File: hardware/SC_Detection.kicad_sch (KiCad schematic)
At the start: 86 parts, among them U23 LT1678CS8#PBF, U24 LT1678CS8#PBF, U25 LM211DRG4, U26 LM211DRG4, U27 LM211DRG4, U28 LM211DRG4

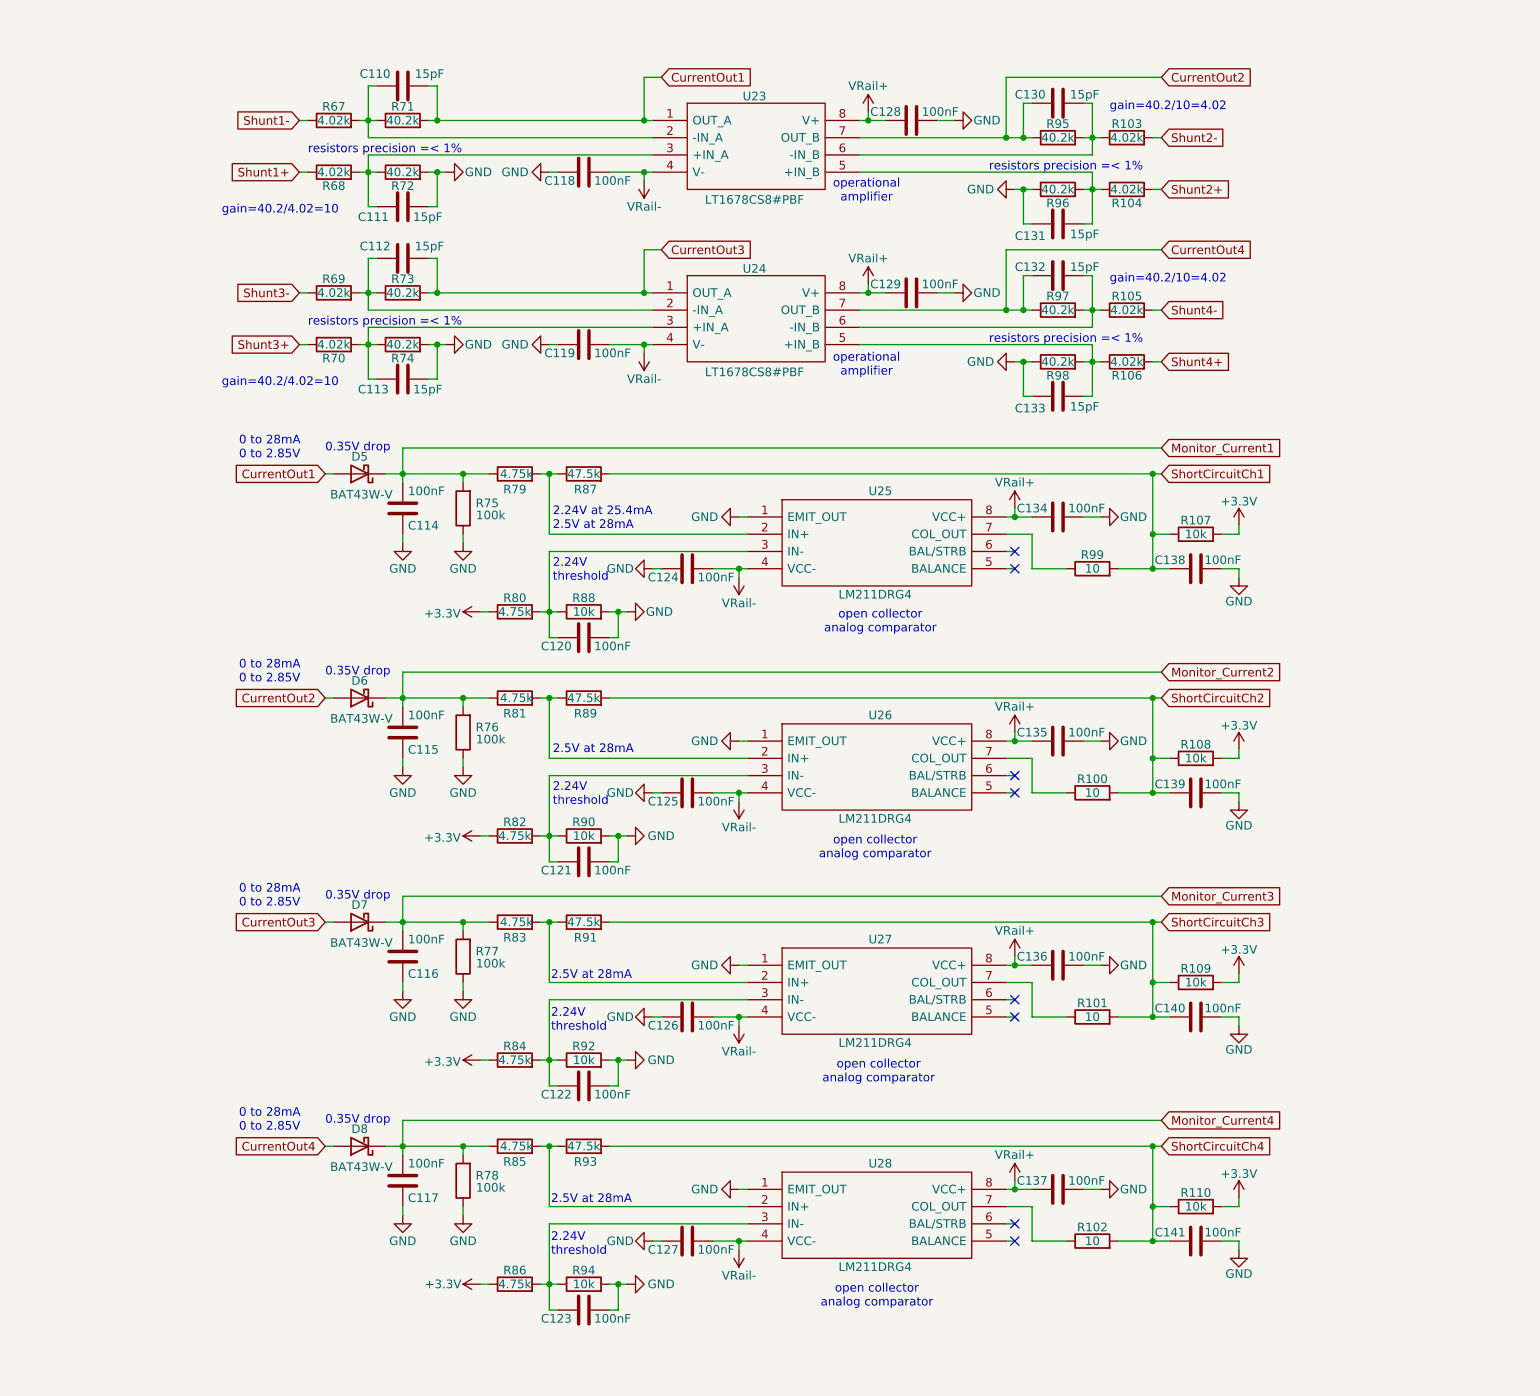
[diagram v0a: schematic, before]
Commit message: Added caps voltage rating + block diagram
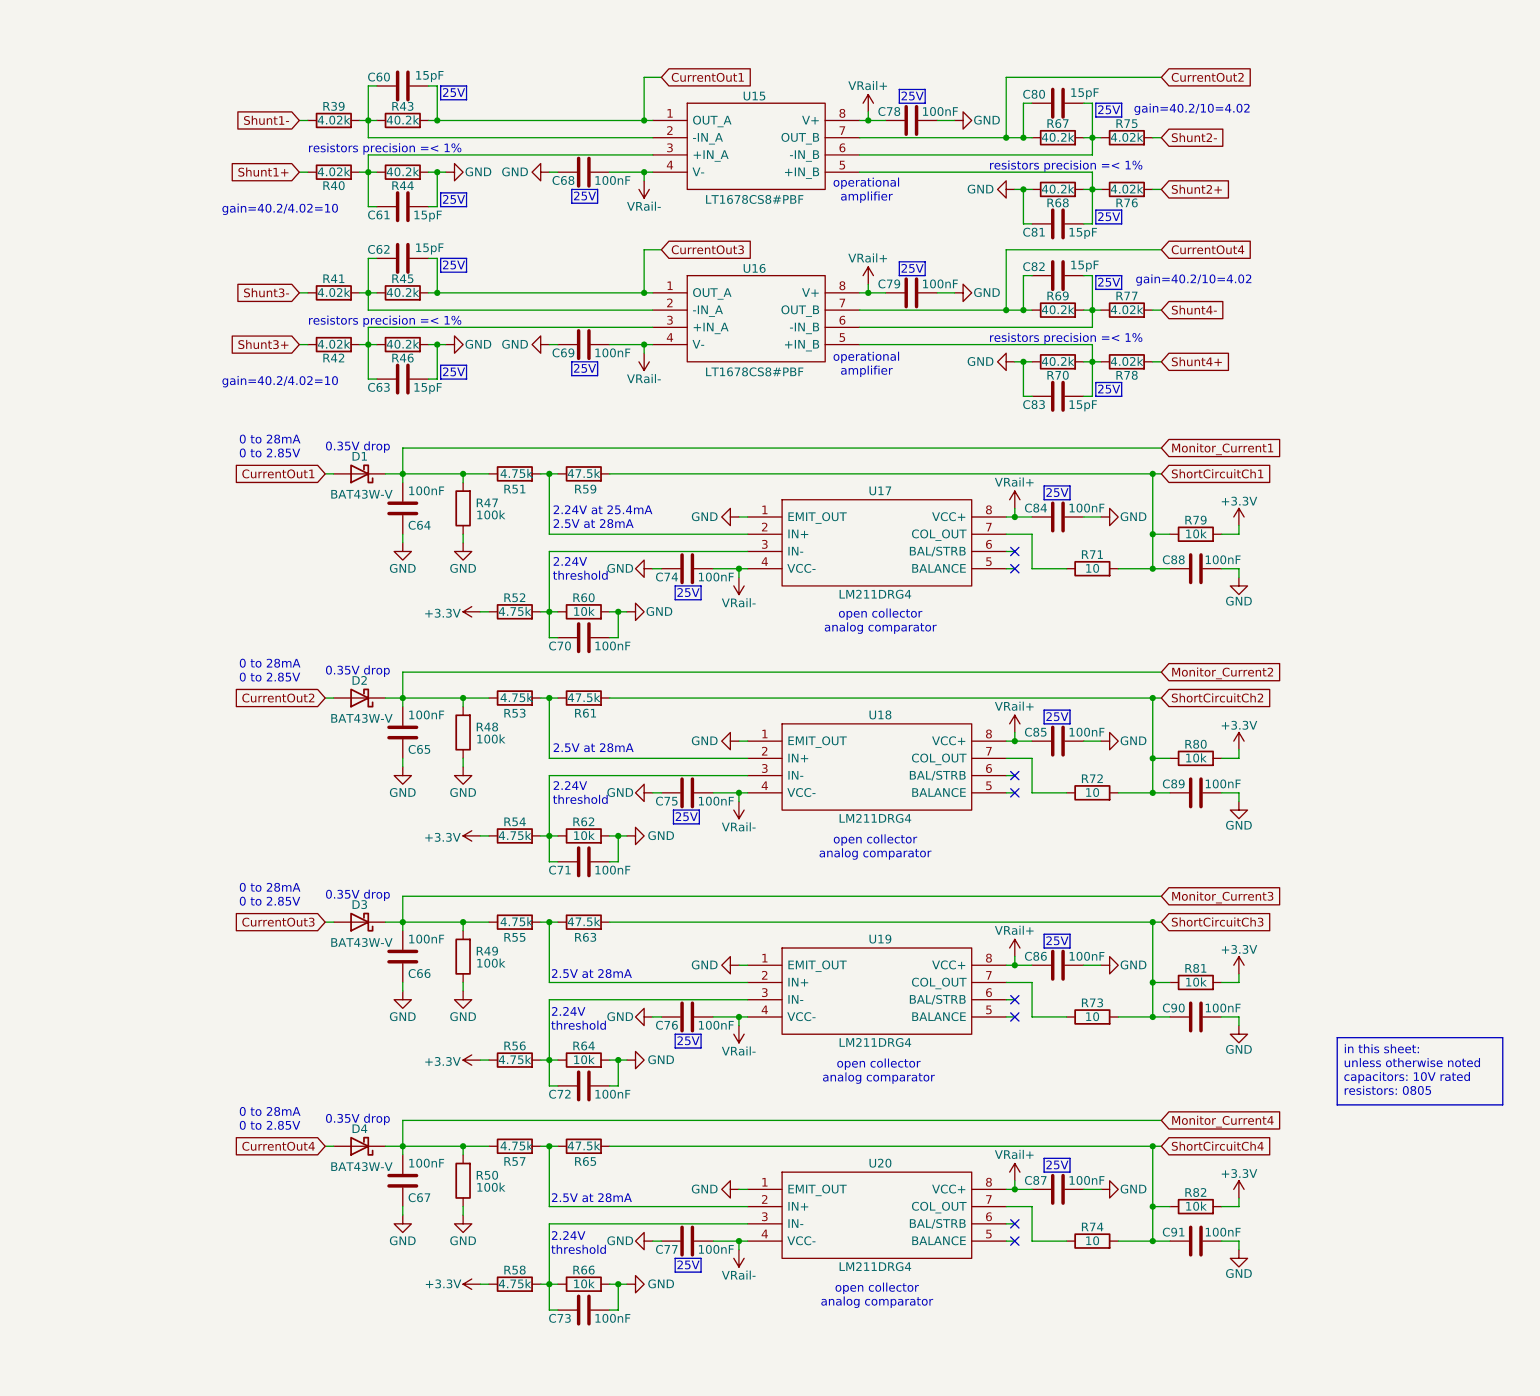
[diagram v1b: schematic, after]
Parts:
- removed C112, C113, C130, C131, C132, C133: 15pF, Capacitor_SMD:C_0402_1005Metric, symbol Device:C
- added C62, C63, C80, C81, C82, C83: 15pF, Capacitor_SMD:C_0402_1005Metric, symbol Device:C
- renumbered C110 to C60, C111 to C61, C114 to C64, C115 to C65, C116 to C66, C117 to C67, C118 to C68, C119 to C69, C120 to C70, C121 to C71, C122 to C72, C123 to C73, C124 to C74, C125 to C75, C126 to C76, C127 to C77, C128 to C78, C129 to C79, C134 to C84, C135 to C85, C136 to C86, C137 to C87, C138 to C88, C139 to C89, C140 to C90, C141 to C91, D5 to D1, D6 to D2, D7 to D3, D8 to D4, R67 to R39, R68 to R40, R69 to R41, R70 to R42, R71 to R43, R72 to R44, R73 to R45, R74 to R46, R75 to R47, R76 to R48, R77 to R49, R78 to R50, R79 to R51, R80 to R52, R81 to R53, R82 to R54, R83 to R55, R84 to R56, R85 to R57, R86 to R58, R87 to R59, R88 to R60, R89 to R61, R90 to R62, R91 to R63, R92 to R64, R93 to R65, R94 to R66, R95 to R67, R96 to R68, R97 to R69, R98 to R70, R99 to R71, R100 to R72, R101 to R73, R102 to R74, R103 to R75, R104 to R76, R105 to R77, R106 to R78, R107 to R79, R108 to R80, R109 to R81, R110 to R82, U23 to U15, U24 to U16, U25 to U17, U26 to U18, U27 to U19, U28 to U20
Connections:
- net CurrentOut2: now also C80.2
- net CurrentOut3: now also C62.1
- net CurrentOut4: now also C82.2
- net GND: now also C63.1, C81.2, C83.2
- net at R67.2, R75.1, U15.6 (-IN_B): now also C80.1
- net at R69.2, R77.1, U16.6 (-IN_B): now also C82.1
- net at R70.2, R78.1, U16.5 (+IN_B): now also C83.1
- net at R41.2, R45.1, U16.2 (-IN_A): now also C62.2
- net at R68.2, R76.1, U15.5 (+IN_B): now also C81.1
- net at R42.2, R46.1, U16.3 (+IN_A): now also C63.2
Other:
- title: Multi Channel HARP DAC -> harp device quad dac

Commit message: The footprint assigning and reviewing have started.
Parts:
- C60, C61, C62, C63, C64, C65, C66, C67, C68, C69, C70, C71, C72, C73, C74, C75, C76, C77, C78, C79, C80, C81, C82, C83, C84, C85, C86, C87, C88, C89, C90, C91: symbol Device:C -> harp.device.quad.dac:C
- D1, D2, D3, D4: symbol Diode:BAT43W-V -> harp.device.quad.dac:BAT43W-V
- R39, R40, R41, R42, R43, R44, R45, R46, R47, R48, R49, R50, R51, R52, R53, R54, R55, R56, R57, R58, R59, R60, R61, R62, R63, R64, R65, R66, R67, R68, R69, R70, R71, R72, R73, R74, R75, R76, R77, R78, R79, R80, R81, R82: symbol Device:R -> harp.device.quad.dac:R
- U15, U16: symbol LT1678CS8#PBF:LT1678CS8#PBF -> harp.device.quad.dac:LT1678CS8#PBF
- U17, U18, U19, U20: symbol LM211DRG4:LM211DRG4 -> harp.device.quad.dac:LM211DRG4

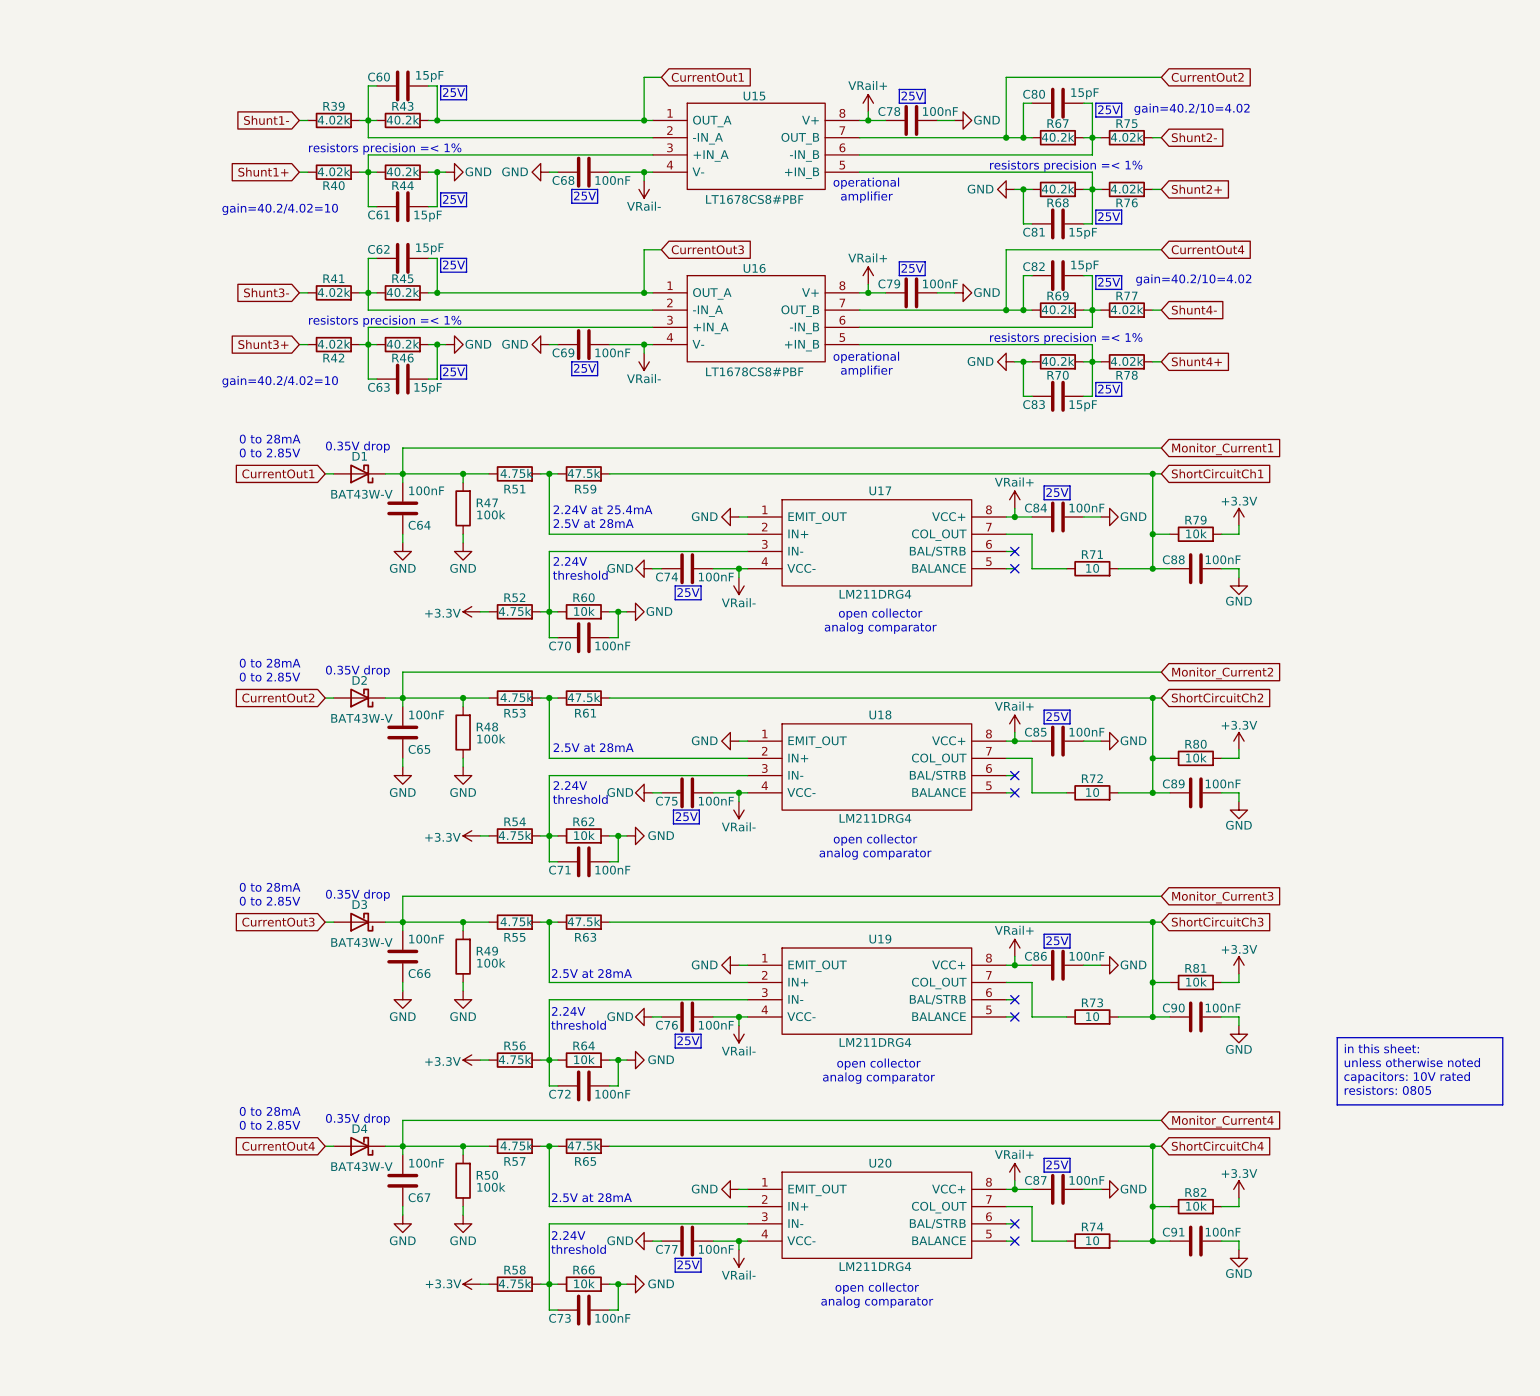
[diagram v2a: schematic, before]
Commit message: Modified notes about caps and resistors
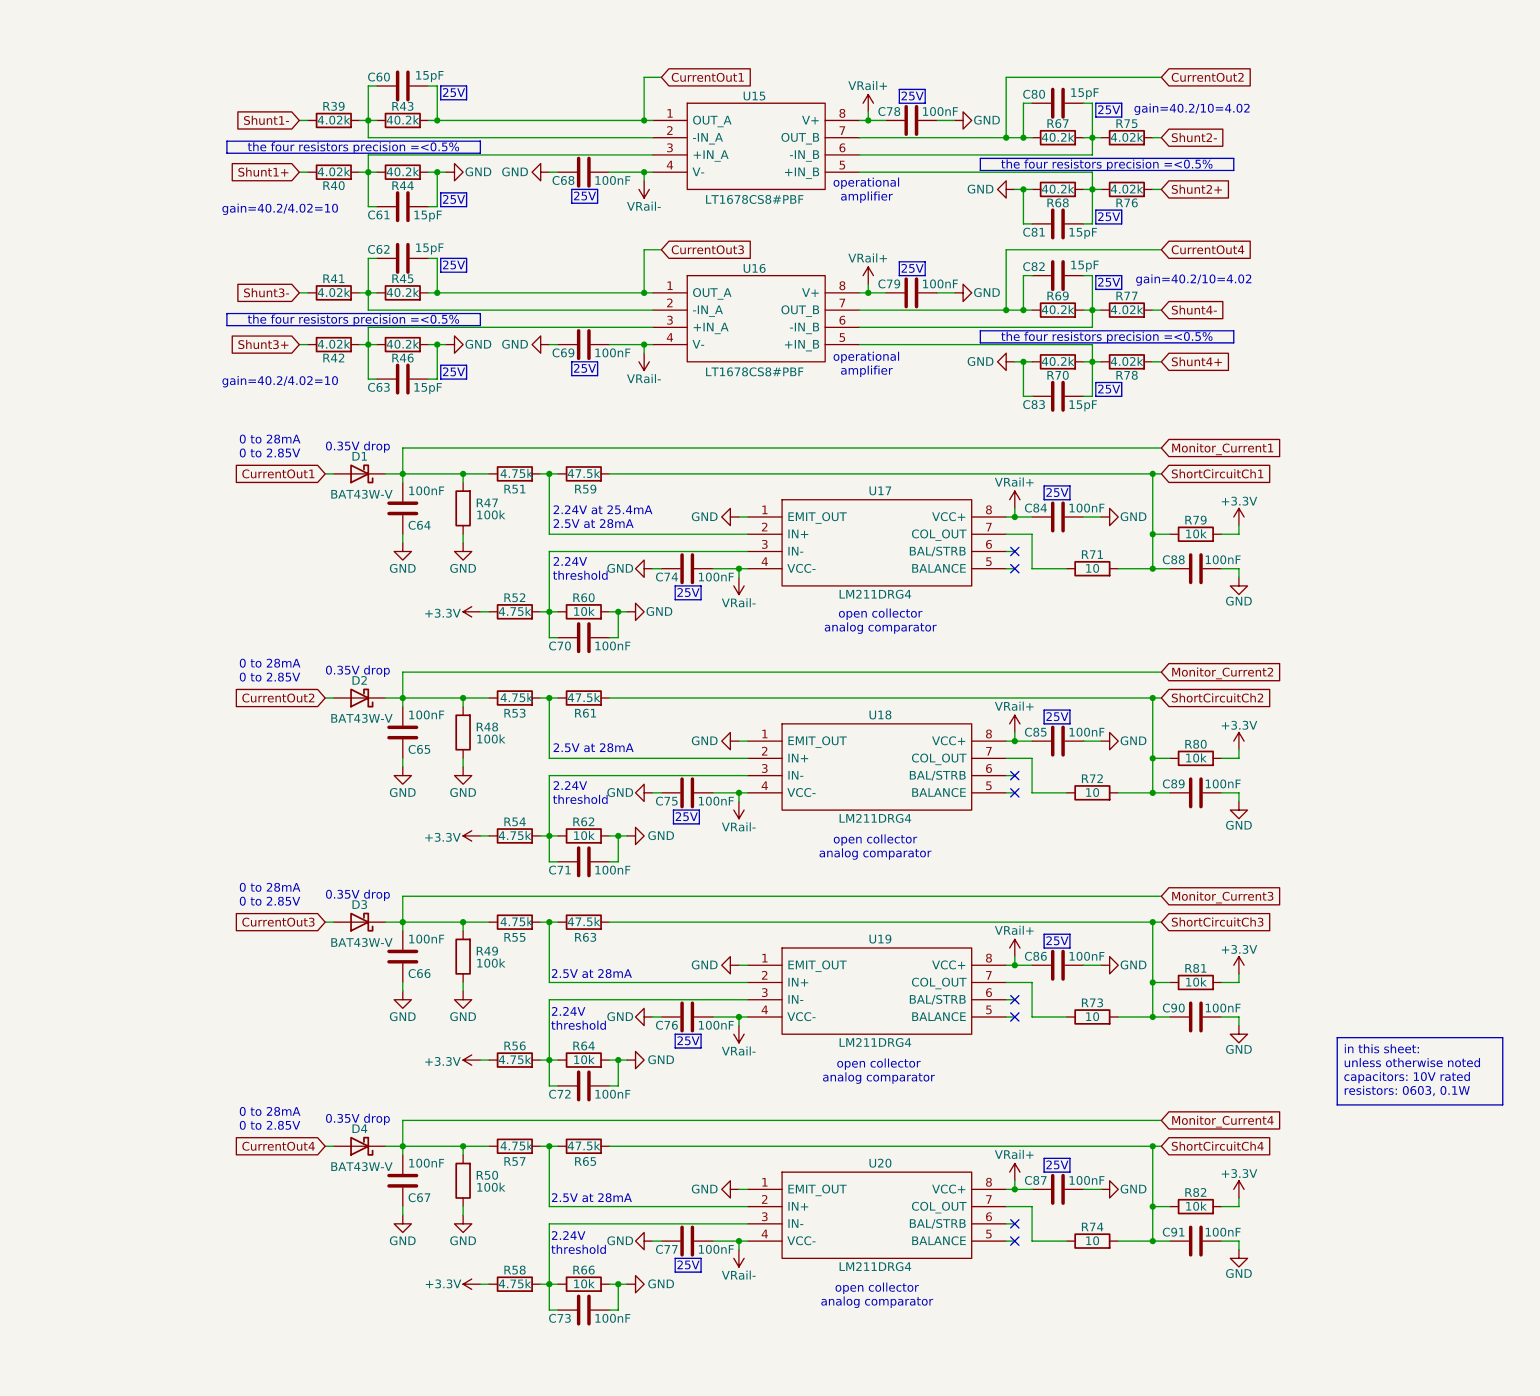
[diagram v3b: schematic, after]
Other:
- note removed: "resistors precision =< 1%"
